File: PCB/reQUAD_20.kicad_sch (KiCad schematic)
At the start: 12 parts, among them J1 Model_100_System_BUS, U1 AS6C1008, U2 74x573, U3 74x2G79, U4 74x02

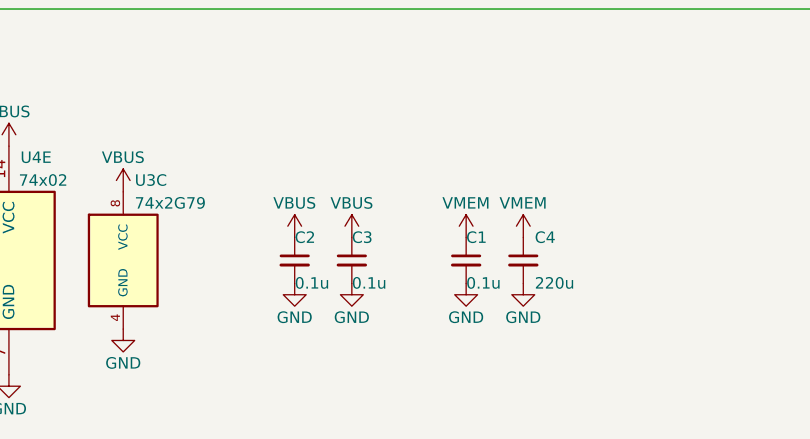
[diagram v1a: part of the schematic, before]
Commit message: tiny pcb layout nudges
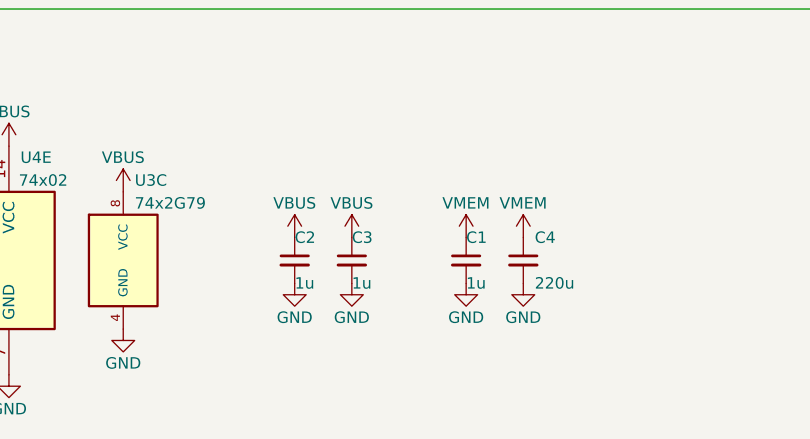
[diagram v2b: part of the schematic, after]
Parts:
- C1, C2, C3: value 0.1u -> 1u
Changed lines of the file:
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@@
       (effects (font (size 1.27 1.27)) (justify left))
     )
-    (property "Value" "0.1u" (at 139.7 186.69 0)
+    (property "Value" "1u" (at 139.7 186.69 0)
       (effects (font (size 1.27 1.27)) (justify left))
     )
@@
       (effects (font (size 1.27 1.27)) (justify left))
     )
-    (property "Value" "0.1u" (at 120.65 186.69 0)
+    (property "Value" "1u" (at 120.65 186.69 0)
       (effects (font (size 1.27 1.27)) (justify left))
     )
@@
       (effects (font (size 1.27 1.27)) (justify left))
     )
-    (property "Value" "0.1u" (at 127 186.69 0)
-      (effects (font (size 1.27 1.27)) (justify left))
-    )
+    (property "Value" "1u" (at 127 186.69 0)
+      (effects (font (size 1.27 1.27)) (justify left))
+    )
